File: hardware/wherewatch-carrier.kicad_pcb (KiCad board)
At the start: 4 copper layers, 37.4 x 26 mm, 33 parts, among them J1 JST_PH_S2B-PH-SM4-TB_1x02-1MP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, J3 U.FL_Hirose_U.FL-R-SMT-1_Vert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, J4 JST_PH_S2B-PH-SM4-TB_1x02-1MP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, J5 JST_PH_S2B-PH-SM4-TB_1x02-1MP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, J6 PinHeader_1x04_P1.00mm_Vertic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, Q1 SOT-23, Q2 SOT-23, Q3 SOT-23, SW1 SW-TH_MSK12C02, SW2 SW_SPST_TL3342, U1 Val**, U2 LGA-14_3x2.5mm_P0.5mm_LayoutB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, U3 GPSM-SMD_ATGM336H-TR, U4 TQFN-16-1EP_3x3mm_P0.5mm_EP1.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

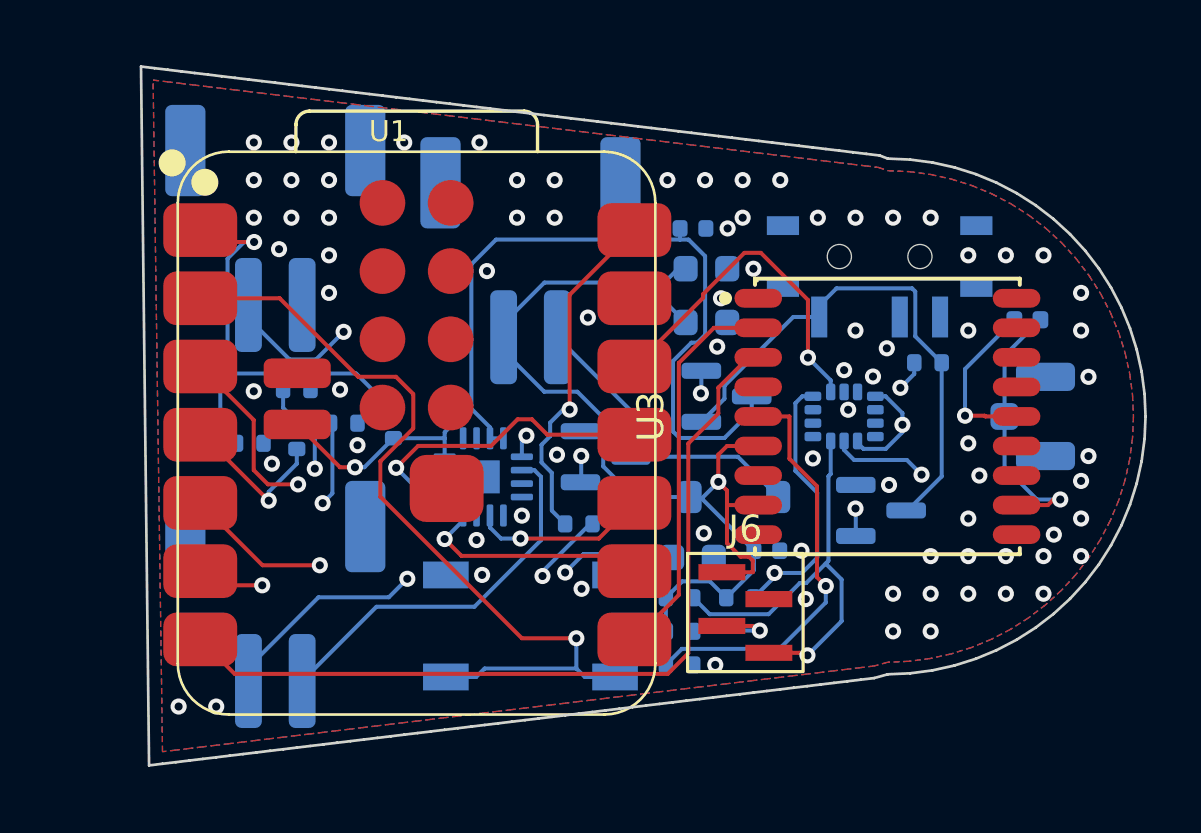
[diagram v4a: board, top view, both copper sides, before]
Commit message: hardware: v0.5 layout, two-sided, JST SH connectors (decision 7); DRC clean
J1, J4, J5 are JST SH SM02B-SRSS-TB (C160402, 2.9 mm tall) instead of
the 5.5 mm PH, so the stack under the board fits the 8.2 to 8.5 mm case
cavity. Two-sided again for Seeed Fusion, who place both faces: GNSS
module, 47 nH, motor FET and diode back on top, the SH 4-pin OLED
connector back on the bottom; only the XIAO remains a Seeed-sourced
module (SKU 113991115). Ground pours now use 0.13 mm clearance and
0.15 mm minimum width; with 0.15/0.25, C4's GND pad sat on a pour
island between traces that no via could reach (DRC: 1 unconnected).

Routed with freerouting 1.9.0 (-mp 300, route-v05a.ses); DRC errors:
0 violations, 0 unconnected. Order files: gerbers-v05.zip, bom-jlc.csv,
bom-seeed.csv (Designator, MPN, Qty, Link), cpl-jlc.csv, and the
assembly-instructions zip Seeed asks for (pick-and-place, renders).

Co-Authored-By: Claude Fable 5.1 <noreply@anthropic.com>
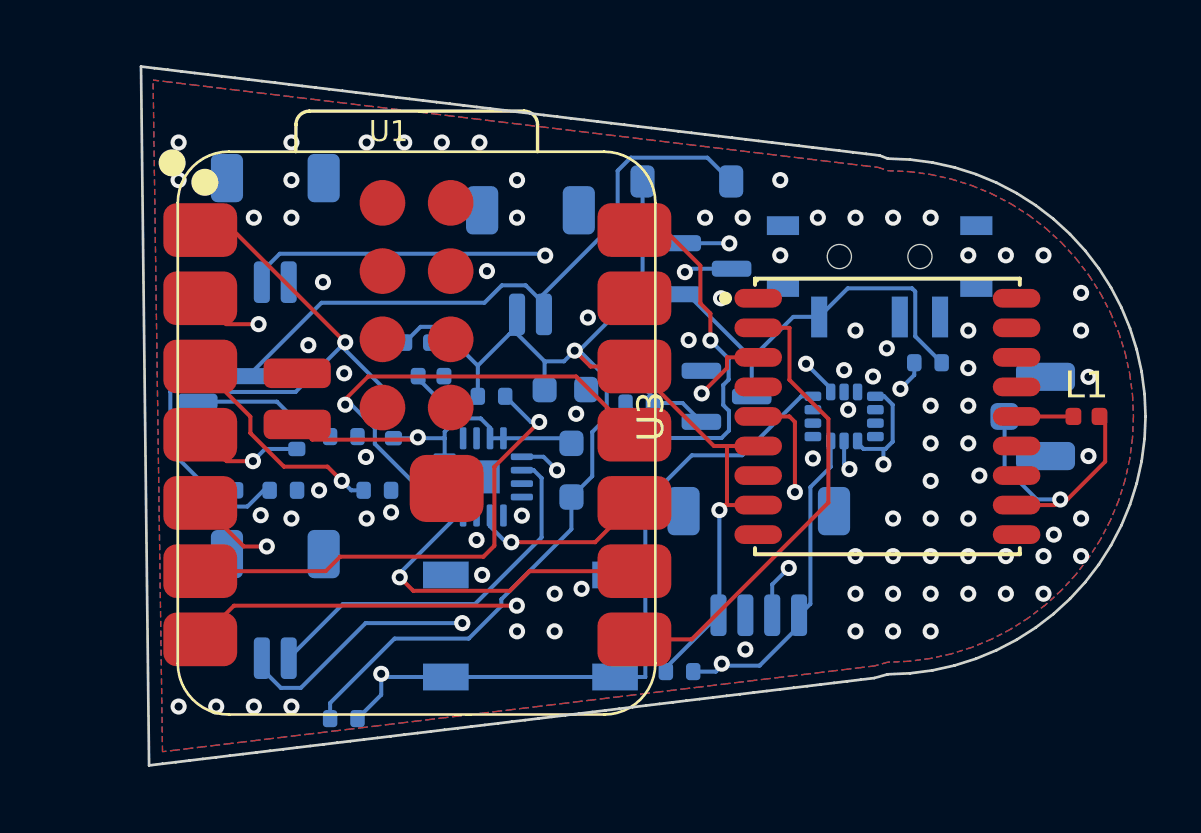
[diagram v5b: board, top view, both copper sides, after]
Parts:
- J1, J4, J5: value JST_PH_S2B-PH-SM4-TB_1x02-1MP_P2.00mm_Horizontal -> JST_SH_SM02B-SRSS-TB_1x02-1MP_P1.00mm_Horizontal; footprint JST_PH_S2B-PH-SM4-TB_1x02-1MP_P2.00mm_Horizontal -> JST_SH_SM02B-SRSS-TB_1x02-1MP_P1.00mm_Horizontal
- J6: value PinHeader_1x04_P1.00mm_Vertical_SMD_Pin1Left -> JST_SH_SM04B-SRSS-TB_1x04-1MP_P1.00mm_Horizontal; footprint OLED_Pads_1x04_P1.00mm -> JST_SH_SM04B-SRSS-TB_1x04-1MP_P1.00mm_Horizontal; moved to B.Cu
- L1: moved to F.Cu
- moved R11 15.4 mm to (21.8, 11.2)
- moved C5 15.1 mm to (24.5, -2.75)
- moved Q3 14.6 mm to (17.2, -1.50)
- moved R9 13.0 mm to (23.0, 2.75)
- moved D1 11.9 mm to (34.5, -8.75)
- moved R5 11.2 mm to (27.2, -0.75)
- moved C3 11.2 mm to (25.0, -1.50)
- moved R10 11.2 mm to (32.8, -1.75)
- moved C6 9.50 mm to (31.0, 3.00)
- moved Q2 7.15 mm to (36.0, -0.75)
- moved C1 5.81 mm to (30.0, -1.00)
- moved C2 5.67 mm to (31.0, 1.00)
- moved R2 5.03 mm to (32.8, -0.50)
- moved Q1 4.81 mm to (35.2, -5.50)
- moved L1 4.22 mm to (49.4, 0.00)
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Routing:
- net VBUS_DET: track 29.0 -> 3.76 mm, vias 3 -> 0
- net VBAT: track 50.8 -> 29.6 mm
- net GNSS_EN: track 46.0 -> 29.5 mm
- net VIB_N: track 11.7 -> 23.9 mm
- net VIB_IN_R: track 15.9 -> 5.47 mm, vias 2 -> 0
- net +3V3: track 67.2 -> 75.0 mm, vias 3 -> 4
- net SDA: track 41.2 -> 34.0 mm
- net I2S_DIN: track 12.1 -> 17.7 mm
- net VBAT_SENSE: track 19.3 -> 24.8 mm
- net GNSS_RX: track 31.3 -> 26.0 mm, vias 0 -> 2
- net BTN: track 49.2 -> 44.6 mm
- net SW_G: track 19.7 -> 15.3 mm
- net VCC_RF: track 6.26 -> 2.12 mm, vias 1 -> 0
- net I2S_BCLK: track 8.72 -> 12.6 mm
- net GNSS_TX: track 14.5 -> 17.6 mm
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
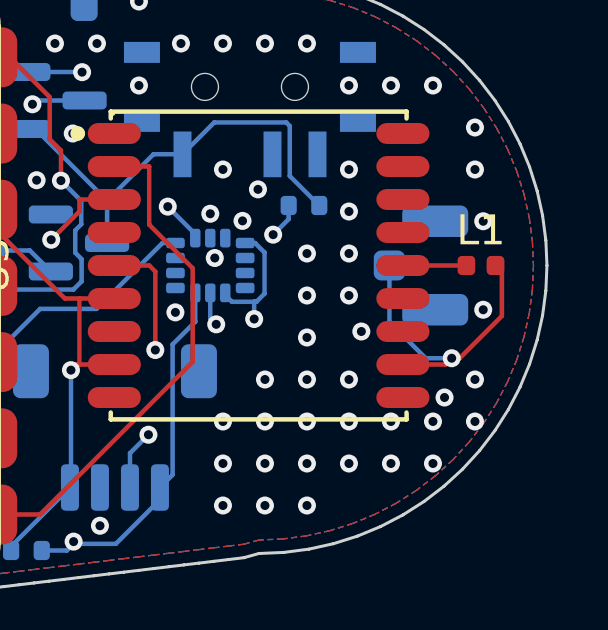
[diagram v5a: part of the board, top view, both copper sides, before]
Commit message: hardware: fix GNSS_RF antenna feed impedance (0.15mm -> 0.35mm, JLC7628 50 ohm)
GNSS_RF (1575 MHz GPS feed) was 9 segments of the board-wide default
0.15mm trace, ~76-83 ohm by IPC-2141/Hammerstad-Jensen on the JLC7628
4-layer 1.6mm stackup (0.2104mm 7628 prepreg, Er 4.4, F.Cu/In1.Cu and
In2.Cu/B.Cu; 1.065mm core, Er 4.6, In1.Cu/In2.Cu; source:
jlcpcb.com/impedance). Measured length was 10.20mm split 5.74mm F.Cu /
4.46mm B.Cu (not the ~4.0/4.5mm estimate in the defect report), through
one via.

Widened every GNSS_RF segment to 0.35mm (IPC-2141 50.0 ohm design
width; Hammerstad-Jensen cross-check 54.3 ohm, ~9% high, both models
agree the fix moves it from ~76-83 ohm down to ~50-54 ohm). The
stackup is symmetric top-to-bottom, so the same width is ~50 ohm on
F.Cu-over-In1.Cu and on B.Cu-over-In2.Cu.

Could not eliminate the via or keep the feed on one layer as originally
asked: J3 (u.FL antenna connector) is an SMD footprint on the BOTTOM
side with its GNSS_RF pad copper only on B.Cu, while U3 (module RF_IN)
and L1 (bias-tee tap) are on F.Cu. A single via is physically required
unless J3 is moved to the top side, which is out of scope for a
surgical edit. Kept the existing via at its original location (already
clearance-proven) and widened both sides instead, so the remaining
discontinuity is just the one via, not a wrong-width run on either
layer. Nudged two waypoints (L1 branch, J3 branch) by <1mm to clear
0.2mm clearance to a nearby GND via and a J3 GND pad at the new width;
no other net's copper was moved.

Added an RF netclass (0.35mm track, pattern GNSS_RF) to
wherewatch-carrier.kicad_pro, and a (setup (stackup ...)) block to
wherewatch-carrier.kicad_pcb recording the JLC7628 numbers above, since
the board previously had no stackup defined.

Verified: pad->net listing is byte-identical before/after (159 pads,
0 differences) - connectivity unchanged. DRC (kicad-cli 10.0.6):
69 violations before and after, all pre-existing silkscreen/text-height
issues unrelated t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
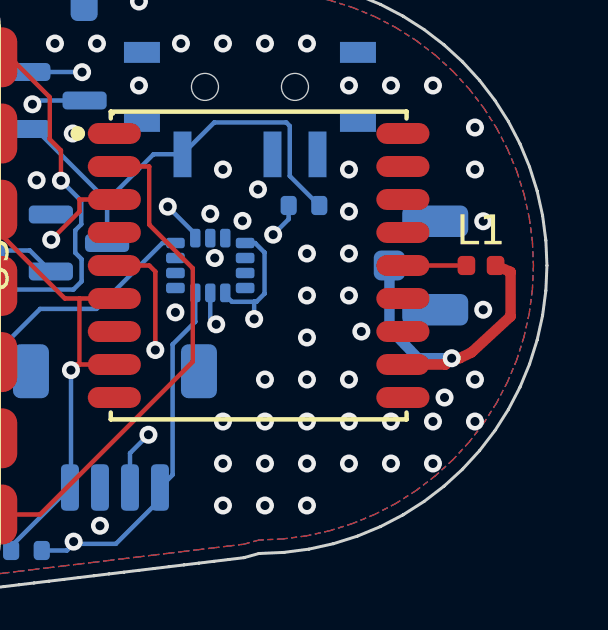
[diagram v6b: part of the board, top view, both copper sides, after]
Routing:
- net GNSS_RF: track 10.2 -> 10.8 mm
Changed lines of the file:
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@@
 	)
 	(setup
+		(stackup
+			(layer "F.SilkS"
+				(type "Top Silk Screen")
+			)
+			(layer "F.Paste"
+				(type "Top Solder Paste")
+			)
+			(layer "F.Mask"
+				(type "Top Solder Mask")
+				(color "Green")
+				(thickness 0.01)
+			)
+			(layer "F.Cu"
+				(type "copper")
+				(thickness 0.035)
+			)
+			(layer "dielectric 1"
+				(type "prepreg")
+				(thickness 0.2104)
+				(material "PP7628")
+				(epsilon_r 4.4)
+				(loss_tangent 0.02)
+			)
+			(layer "In1.Cu"
+				(type "copper")
+				(thickness 0.0152)
+			)
+			(layer "dielectric 2"
+				(type "core")
+				(thickness 1.065)
+				(material "FR4")
+				(epsilon_r 4.6)
+				(loss_tangent 0.02)
+			)
+			(layer "In2.Cu"
+				(type "copper")
+				(thickness 0.0152)
+			)
+			(layer "dielectric 3"
+				(type "prepreg")
+				(thickness 0.2104)
+				(material "PP7628")
+				(epsilon_r 4.4)
+				(loss_tangent 0.02)
+			)
+			(layer "B.Cu"
+				(type "copper")
+				(thickness 0.035)
+			)
+			(layer "B.Mask"
+				(type "Bottom Solder Mask")
+				(color "Green")
+				(thickness 0.01)
+			)
+			(layer "B.Paste"
+				(type "Bottom Solder Paste")
+			)
+			(layer "B.SilkS"
+				(type "Bottom Silk Screen")
+			)
+			(copper_finish "None")
+			(dielectric_constraints no)
+		)
 		(pad_to_mask_clearance 0)
 		(allow_soldermask_bridges_in_footprints no)
@@
 	)
 	(segment
-		(start 48.4247 3.0913)
-		(end 48.216 3.3)
-		(width 0.15)
+		(start 48.425 3.091)
+		(end 48.689 3.091)
+		(width 0.35)
 		(layer "F.Cu")
 		(net "GNSS_RF")
 	)
 	(segment
-		(start 48.6892 3.0913)
-		(end 50.0981 1.6824)
-		(width 0.15)
+		(start 48.216 3.3)
+		(end 46.799 3.3)
+		(width 0.35)
 		(layer "F.Cu")
 		(net "GNSS_RF")
 	)
 	(segment
-		(start 48.4247 3.0913)
-		(end 48.6892 3.0913)
-		(width 0.15)
+		(start 49.086 2.897)
+		(end 50.386 1.697)
+		(width 0.35)
 		(layer "F.Cu")
 		(net "GNSS_RF")
 	)
 	(segment
-		(start 48.216 3.3)
-		(end 46.7993 3.3)
-		(width 0.15)
+		(start 50.386 0.213)
+		(end 49.885 0)
+		(width 0.35)
 		(layer "F.Cu")
 		(net "GNSS_RF")
 	)
 	(segment
-		(start 50.0981 1.6824)
-		(end 50.0981 0.2131)
-		(width 0.15)
+		(start 50.386 1.697)
+		(end 50.386 0.213)
+		(width 0.35)
 		(layer "F.Cu")
 		(net "GNSS_RF")
 	)
 	(segment
-		(start 50.0981 0.2131)
-		(end 49.885 0)
-		(width 0.15)
+		(start 48.425 3.091)
+		(end 48.216 3.3)
+		(width 0.35)
+		(layer "F.Cu")
+		(net "GNSS_RF")
+	)
+	(segment
+		(start 48.689 3.091)
+		(end 49.086 2.897)
+		(width 0.35)
 		(layer "F.Cu")
 		(net "GNSS_RF")
@@
 	)
 	(segment
-		(start 46.35 1.8826)
-		(end 47.5587 3.0913)
-		(width 0.15)
+		(start 46.35 0)
+		(end 46.35 2.1)
+		(width 0.35)
 		(layer "B.Cu")
 		(net "GNSS_RF")
 	)
 	(segment
-		(start 46.35 0)
-		(end 46.35 1.8826)
-		(width 0.15)
+		(start 46.35 2.1)
+		(end 47.3 3.091)
+		(width 0.35)
 		(layer "B.Cu")
 		(net "GNSS_RF")
 	)
 	(segment
-		(start 47.5587 3.0913)
-		(end 48.4247 3.0913)
-		(width 0.15)
+		(start 47.3 3.091)
+		(end 48.425 3.091)
+		(width 0.35)
 		(layer "B.Cu")
 		(net "GNSS_RF")
